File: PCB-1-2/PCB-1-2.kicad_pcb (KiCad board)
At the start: 2 copper layers, 89 x 51.5 mm, 97 parts, among them J1 Bus_PCI_Express_x8, J2 ST STDC14 (Debug Connector), J3 USB4105-GF-A, U1 LTC1298IS8_PBF, U10 INA827AIDGKR, U11 LTC1250CS8-PBF, U12 REF3425MDBVTEP, U13 HI-3585APQI, U14 MAX764ESA, U2 LTC1451IS8-PBF, U3 HI-3110PSIF, U4 FT231XS-R, U5 STM32F103RBT6, U6 STWD100YNXWY3F, U7 ADP7104ACPZ-R7 (v3.3), U8 OPA2187IDGKR, U9 ADP7104ACPZ-R7 (5v), Y1 8MHz Crystal, Y2 ABM8-24.000MHz-10-B1U-T

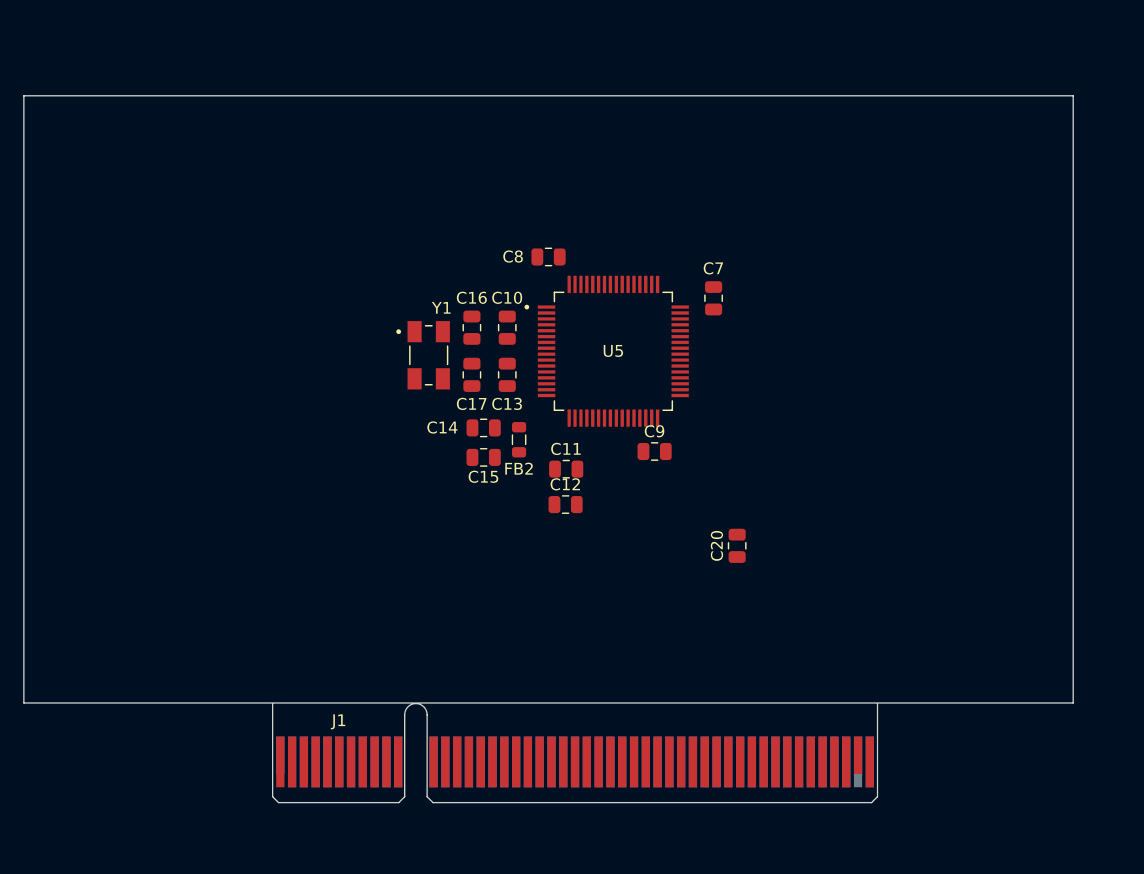
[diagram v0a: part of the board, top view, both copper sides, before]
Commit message: Fixing PCIe simple, not done yet
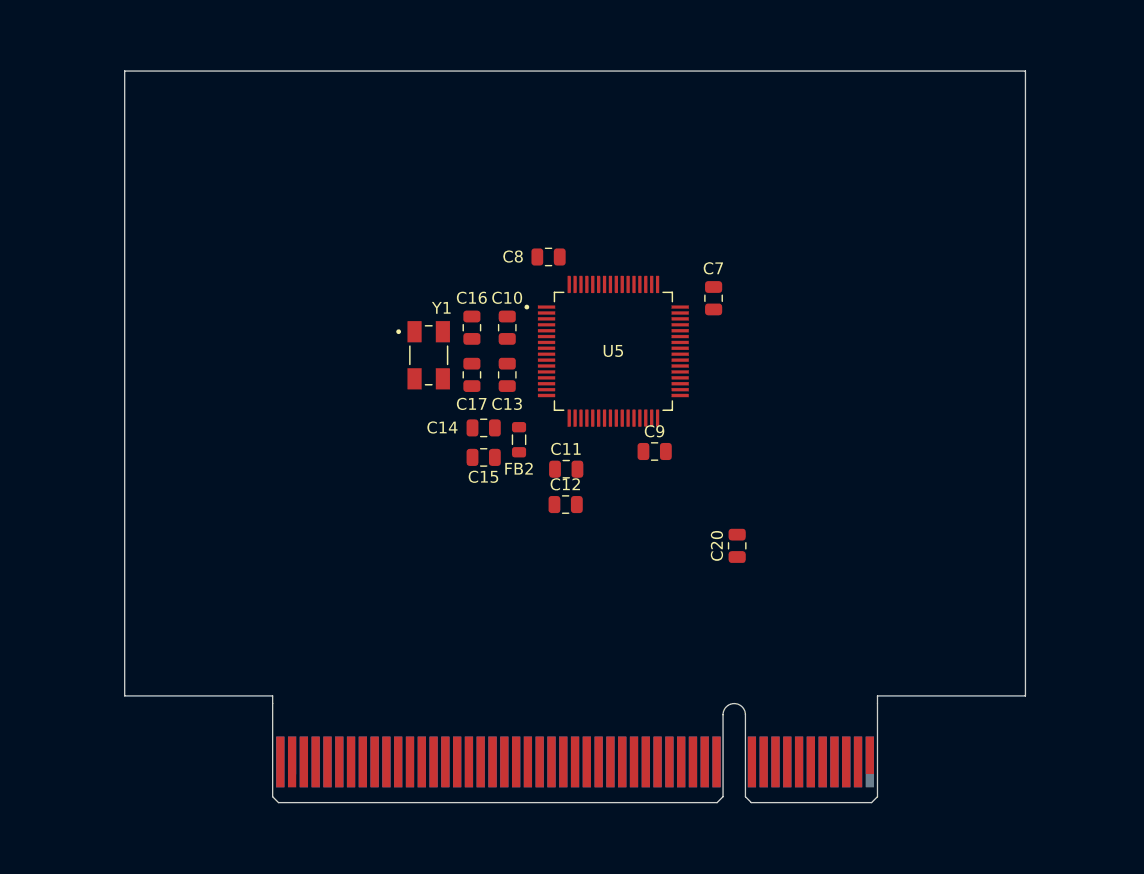
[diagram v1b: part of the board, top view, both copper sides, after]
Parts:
- C18, C19: value 4.7uF -> 22uF
- J1: moved to B.Cu
- moved J1 50.0 mm to (123.0, 131.0), turned to 180 degrees
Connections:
- C1 pad 2: GND -> Transducer-
- C10 pad 1: GND -> Transducer-
- C11 pad 1: GND -> Transducer-
- C12 pad 1: GND -> Transducer-
- C13 pad 2: GND -> Transducer-
- C14 pad 2: GND -> Transducer-
- C15 pad 2: GND -> Transducer-
- C16 pad 2: GND -> Transducer-
- C17 pad 2: GND -> Transducer-
- C18 pad 2: GND -> Transducer-
- C19 pad 2: GND -> Transducer-
- C2 pad 1: Net-(U2-VCC) -> +5V
- C2 pad 2: GND -> Transducer-
- C20 pad 2: GND -> Transducer-
- C21 pad 2: GND -> Transducer-
- C22 pad 2: GND -> Transducer-
- C23 pad 2: GND -> Transducer-
- C24 pad 1: GND -> Transducer-
- C26 pad 2: GND -> Transducer-
- C27 pad 2: GND -> Transducer-
- C28 pad 2: GND -> Transducer-
- C3 pad 2: GND -> Transducer-
- C30 pad 2: GND -> Transducer-
- C31 pad 2: GND -> Transducer-
- C32 pad 2: GND -> Transducer-
- C33 pad 2: GND -> Transducer-
- C34 pad 2: GND -> Transducer-
- C35 pad 2: GND -> Transducer-
- C36 pad 1: GND -> Transducer-
- C37 pad 1: GND -> Transducer-
- C38 pad 1: GND -> Transducer-
- C39 pad 2: GND -> Transducer-
- C4 pad 2: GND -> Transducer-
- C40 pad 2: GND -> Transducer-
- C41 pad 2: GND -> Transducer-
- C42 pad 1: GND -> Transducer-
- C43 pad 1: GND -> Transducer-
- C44 pad 1: GND -> Transducer-
- C45 pad 2: GND -> Transducer-
- C46 pad 2: GND -> Transducer-
- C5 pad 2: GND -> Transducer-
- C6 pad 1: GND -> Transducer-
- C7 pad 1: GND -> Transducer-
- C8 pad 1: GND -> Transducer-
- C9 pad 1: GND -> Transducer-
- D1 pad 1: GND -> Transducer-
- J2 pad 05: GND -> Transducer-
- J2 pad 07: GND -> Transducer-
- J2 pad 11: GND -> Transducer-
- J3 pad A1_B12: GND -> Transducer-
- J3 pad B1_A12: GND -> Transducer-
- J3 pad SH1: GND -> Transducer-
- J3 pad SH2: GND -> Transducer-
- J3 pad SH3: GND -> Transducer-
- J3 pad SH4: GND -> Transducer-
- R1 pad 2: GND -> Transducer-
- R18 pad 2: GND -> Transducer-
- R24 pad 2: GND -> Transducer-
- R25 pad 2: GND -> Transducer-
- R26 pad 2: GND -> Transducer-
- R7 pad 1: GND -> Transducer-
- R9 pad 1: GND -> Transducer-
- U1 pad 1: SPI1_CS -> SPI2_CS
- U1 pad 4: GND -> Transducer-
- U10 pad 5: GND -> Transducer-
- U10 pad 6: GND -> Transducer-
- U11 pad 4: GND -> Transducer-
- U12 pad 1: GND -> Transducer-
- U12 pad 2: GND -> Transducer-
- U13 pad 9: SPI1_CS -> SPI2_CS
- U14 pad 1: unconnected-(U14-OUT-Pad1) -> -5V
- U14 pad 2: unconnected-(U14-FB-Pad2) -> Net-(U14-FB)
- U14 pad 3: unconnected-(U14-SHDN-Pad3) -> Transducer-
- U14 pad 4: unconnected-(U14-REF-Pad4) -> Net-(U14-FB)
- U14 pad 5: unconnected-(U14-GND-Pad5) -> Transducer-
- U14 pad 6: unconnected-(U14-V+-Pad6) -> +5V
- U14 pad 7: unconnected-(U14-V+-Pad7) -> +5V
- U14 pad 8: unconnected-(U14-LX-Pad8) -> Net-(D2-K)
- U2 pad 3: SPI1_CS -> SPI2_CS
- U2 pad 5: GND -> Transducer-
- U2 pad 8: Net-(U2-VCC) -> +5V
- U3 pad 8: GND -> Transducer-
- U4 pad 16: GND -> Transducer-
- U4 pad 6: GND -> Transducer-
- U5 pad 12: GND -> Transducer-
- U5 pad 18: GND -> Transducer-
- U5 pad 31: GND -> Transducer-
- U5 pad 33: SPI1_CS -> SPI2_CS
- U5 pad 34: SPI2_CLK -> SPI2_SCK
- U5 pad 47: GND -> Transducer-
- U5 pad 60: GND -> Transducer-
- U5 pad 63: GND -> Transducer-
- U6 pad 2: GND -> Transducer-
- U7 pad 3: GND -> Transducer-
- U7 pad 6: GND -> Transducer-
- U7 pad 9: GND -> Transducer-
- U8 pad 4: GND -> Transducer-
- U9 pad 3: GND -> Transducer-
- U9 pad 6: GND -> Transducer-
- U9 pad 9: GND -> Transducer-
- Y1 pad 2: GND -> Transducer-
- Y1 pad 4: GND -> Transducer-
- Y2 pad 2: GND -> Transducer-
- Y2 pad 4: GND -> Transducer-
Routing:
- net Transducer-: track 0.00 -> 13.0 mm
- net GND: track 13.0 -> 0.00 mm
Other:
- board size 89 x 51.5 mm -> 76.4 x 53.6 mm
- copper layers 2 -> 4

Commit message: Merged both -1/-2 and backplane
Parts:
- removed the R1 at (111.3, 54.8)
- added C47: .1uF, Capacitor_SMD:C_0603_1608Metric, F.Cu at (95.1, 74.6)
- added C48: 22uF, Capacitor_SMD:C_0805_2012Metric, F.Cu at (93.7, 68.1)
- added C49: 22uF, Capacitor_SMD:C_0805_2012Metric, B.Cu at (93.6, 68.1)
- added C50: .1uF, Capacitor_SMD:C_0603_1608Metric, F.Cu at (106.1, 75.4)
- added C51: 10uF, Capacitor_SMD:C_1206_3216Metric, B.Cu at (110.6, 70.6)
- added C52: 22uF, Capacitor_SMD:C_0805_2012Metric, F.Cu at (93.6, 71.6)
- added C53: 2.2uF, Capacitor_SMD:C_0805_2012Metric, B.Cu at (93.6, 71.6)
- added C54: 22uF, Capacitor_SMD:C_0805_2012Metric, F.Cu at (106.2, 72.1)
- added C55: 200pF, Capacitor_SMD:C_0603_1608Metric, B.Cu at (131.0, 106.5)
- added C56: 20pF, Capacitor_SMD:C_0805_2012Metric, B.Cu at (124.6, 103.8)
- added C57: 20pF, Capacitor_SMD:C_0805_2012Metric, F.Cu at (133.5, 103.7)
- added C58: 330nF, Capacitor_SMD:C_0805_2012Metric, B.Cu at (121.5, 123.5)
- added C59: 22uF, Capacitor_SMD:C_0805_2012Metric, B.Cu at (106.1, 72.1)
- added C60: 22uF, Capacitor_SMD:C_0805_2012Metric, F.Cu at (106.1, 68.6)
- added C61: 22uF, Capacitor_SMD:C_0805_2012Metric, B.Cu at (106.1, 68.6)
- added C62: 22uF, Capacitor_SMD:C_0805_2012Metric, F.Cu at (110.1, 70.6)
- added D2: 1N5817, SDII LIB:1N5817, F.Cu at (106.5, 64.1)
- added D3: LED, LED_SMD:LED_0805_2012Metric, F.Cu at (76.8, 72.0)
- added D4: LED, LED_SMD:LED_0805_2012Metric, F.Cu at (82.6, 73.8)
- added D5: GPIO_LED, LED_SMD:LED_0805_2012Metric, F.Cu at (107.5, 106.5)
- added FB1: 120R, Inductor_SMD:L_0805_2012Metric, B.Cu at (76.6, 68.1)
- added H1: MountingHole, MountingHole:MountingHole_2.2mm_M2, F.Cu at (134.7, 124.0)
- added H2: MountingHole, MountingHole:MountingHole_2.2mm_M2, F.Cu at (61.2, 123.9)
- added H3: MountingHole, MountingHole:MountingHole_2.2mm_M2, F.Cu at (134.7, 61.5)
- added H4: MountingHole, MountingHole:MountingHole_2.2mm_M2, F.Cu at (61.2, 61.4)
- added J4: Conn_01x02_Pin, SDII LIB:pin header, F.Cu at (61.5, 100.5)
- added L2: 47uH, LED_SMD:LED_0805_2012Metric, F.Cu at (102.2, 67.5)
- added R28: 1.2k, Resistor_SMD:R_0805_2012Metric, F.Cu at (107.5, 103.0)
- added R30: 30, Resistor_SMD:R_0603_1608Metric, F.Cu at (65.0, 97.0)
- added R31: 30, Resistor_SMD:R_0603_1608Metric, F.Cu at (65.0, 107.0)
- added R32: 30, Resistor_SMD:R_0603_1608Metric, B.Cu at (65.0, 97.0)
- added R33: 30, Resistor_SMD:R_0603_1608Metric, B.Cu at (65.0, 107.0)
- C10, C11, C12, C13, C14, C15, C20, C38, C39, C4, C40, C41, C42, C43, C44, C5, FB2, R1, R10, R12, R15, R17, R19, R21, R22, R24, R25, R26, R27, R29, R4, R5, R6, R8, U6: moved to B.Cu
- C22: value 332nF -> 2nF; footprint Capacitor_SMD:C_0805_2012Metric -> Capacitor_SMD:C_0603_1608Metric
- C23: footprint Capacitor_SMD:C_0805_2012Metric -> Capacitor_SMD:C_0402_1005Metric
- C29: value 400pF -> 200pF; footprint Capacitor_SMD:C_0805_2012Metric -> Capacitor_SMD:C_0603_1608Metric
- C30, C31: value 40pF -> 20pF
- R34: renamed from R28; value 2k -> 1.2k
- moved C38 225.9 mm to (88.2, 94.9), turned to -135 degrees
- moved U6 223.7 mm to (90.5, 97.0), turned to -135 degrees
- moved R27 211.8 mm to (96.5, 90.0), turned to -135 degrees
- moved R34 207.8 mm to (63.0, 73.4), turned to -90 degrees
- moved D1 205.3 mm to (63.0, 76.9), turned to 90 degrees
- moved U14 203.3 mm to (97.5, 69.7)
- moved R10 178.6 mm to (106.1, 121.0), turned to 180 degrees
- moved U7 177.0 mm to (106.1, 120.9), turned to -90 degrees
- moved C19 171.7 mm to (105.9, 117.7), turned to 180 degrees
- moved R8 168.7 mm to (106.6, 116.7), turned to -90 degrees
- moved R9 167.2 mm to (105.9, 115.7), turned to 0 degrees
- moved R5 163.5 mm to (110.4, 120.9), turned to 180 degrees
- moved U9 162.4 mm to (110.3, 120.9), turned to -90 degrees
- moved C18 157.3 mm to (110.1, 117.6), turned to 180 degrees
- moved R6 153.9 mm to (111.0, 116.6), turned to -90 degrees
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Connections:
- C1 pad 2: Transducer- -> GND
- C10 pad 1: Transducer- -> GND
- C11 pad 1: Transducer- -> GND
- C12 pad 1: Transducer- -> GND
- C13 pad 2: Transducer- -> GND
- C14 pad 2: Transducer- -> GND
- C15 pad 2: Transducer- -> GND
- C16 pad 2: Transducer- -> GND
- C17 pad 2: Transducer- -> GND
- C18 pad 2: Transducer- -> GND
- C19 pad 2: Transducer- -> GND
- C2 pad 2: Transducer- -> GND
- C20 pad 2: Transducer- -> GND
- C21 pad 2: Transducer- -> GND
- C22 pad 2: Transducer- -> GND
- C23 pad 2: Transducer- -> GND
- C24 pad 1: Transducer- -> GND
- C26 pad 2: Transducer- -> GND
- C27 pad 2: Transducer- -> GND
- C28 pad 2: Transducer- -> GND
- C3 pad 2: Transducer- -> GND
- C30 pad 2: Transducer- -> GND
- C31 pad 2: Transducer- -> GND
- C32 pad 2: Transducer- -> GND
- C33 pad 2: Transducer- -> GND
- C34 pad 2: Transducer- -> GND
- C35 pad 2: Transducer- -> GND
- C36 pad 1: Transducer- -> GND
- C37 pad 1: Transducer- -> GND
- C38 pad 1: Transducer- -> GND
- C39 pad 2: Transducer- -> GND
- C4 pad 2: Transducer- -> GND
- C40 pad 2: Transducer- -> GND
- C41 pad 2: Transducer- -> GND
- C42 pad 1: Transducer- -> GND
- C43 pad 1: Transducer- -> GND
- C44 pad 1: Transducer- -> GND
- C45 pad 2: Transducer- -> GND
- C46 pad 2: Transducer- -> GND
- C5 pad 2: Transducer- -> GND
- C6 pad 1: Transducer- -> GND
- C7 pad 1: Transducer- -> GND
- C8 pad 1: Transducer- -> GND
- C9 pad 1: Transducer- -> GND
- D1 pad 1: Transducer- -> GND
- J1 pad A10: Net-(J1-+3.3V-PadA10) -> 429_IN-
- J1 pad A11: unconnected-(J1-~{PERST}-PadA11) -> 429_IN+
- J1 pad A12: Net-(J1-GND-PadA12) -> 429_OUT+
- J1 pad A13: unconnected-(J1-REFCLK+-PadA13) -> 429_OUT-
- J1 pad A15: Net-(J1-GND-PadA12) -> unconnected-(J1-Serial-PadA15)
- J1 pad A16: unconnected-(J1-PERp0-PadA16) -> GND
- J1 pad A17: unconnected-(J1-PERn0-PadA17) -> V+_FROM_PCIE
- J1 pad A18: Net-(J1-GND-PadA12) -> GND
- J1 pad A19: unconnected-(J1-RSVD-PadA19) -> DISCRETE_INPUT_1
- J1 pad A2: Net-(J1-+12V-PadA2) -> Transducer+
- J1 pad A20: Net-(J1-GND-PadA12) -> DISCRETE_INPUT_2
- J1 pad A21: unconnected-(J1-PERp1-PadA21) -> DISCRETE_INPUT_3
- J1 pad A22: unconnected-(J1-PERn1-PadA22) -> DISCRETE_INPUT_4
- J1 pad A23: Net-(J1-GND-PadA12) -> DISCRETE_INPUT_5
- J1 pad A24: Net-(J1-GND-PadA12) -> DISCRETE_INPUT_6
- J1 pad A25: unconnected-(J1-PERp2-PadA25) -> GND
- J1 pad A26: unconnected-(J1-PERn2-PadA26) -> GND
- J1 pad A27: Net-(J1-GND-PadA12) -> DISCRETE_OUTPUT_1
- J1 pad A28: Net-(J1-GND-PadA12) -> DISCRETE_OUTPUT_2
- J1 pad A29: unconnected-(J1-PERp3-PadA29) -> DISCRETE_OUTPUT_3
- J1 pad A3: Net-(J1-+12V-PadA2) -> RTD-
- J1 pad A30: unconnected-(J1-PERn3-PadA30) -> DISCRETE_OUTPUT_4
- J1 pad A31: Net-(J1-GND-PadA12) -> DISCRETE_OUTPUT_5
- J1 pad A32: unconnected-(J1-RSVD-PadA32) -> DISCRETE_OUTPUT_6
- J1 pad A33: unconnected-(J1-RSVD-PadA33) -> GND
- J1 pad A34: Net-(J1-GND-PadA12) -> HW_ID_1
- J1 pad A35: unconnected-(J1-PERp4-PadA35) -> HW_ID_2
- J1 pad A36: unconnected-(J1-PERn4-PadA36) -> HW_ID_3
- J1 pad A37: Net-(J1-GND-PadA12) -> unconnected-(J1-GND-PadA37)
- J1 pad A38: Net-(J1-GND-PadA12) -> unconnected-(J1-GND-PadA38)
- J1 pad A4: Net-(J1-GND-PadA12) -> RTD+
- J1 pad A41: Net-(J1-GND-PadA12) -> unconnected-(J1-GND-PadA41)
- J1 pad A42: Net-(J1-GND-PadA12) -> unconnected-(J1-GND-PadA42)
- J1 pad A45: Net-(J1-GND-PadA12) -> unconnected-(J1-GND-PadA45)
- J1 pad A46: Net-(J1-GND-PadA12) -> unconnected-(J1-GND-PadA46)
- J1 pad A49: Net-(J1-GND-PadA12) -> unconnected-(J1-GND-PadA49)
- J1 pad A5: unconnected-(J1-JTAG2-PadA5) -> DAC_OUT
- J1 pad A6: unconnected-(J1-JTAG3-PadA6) -> GND
- J1 pad A7: unconnected-(J1-JTAG4-PadA7) -> 825_CANL
- J1 pad A8: unconnected-(J1-JTAG5-PadA8) -> 825_CANH
- J1 pad A9: Net-(J1-+3.3V-PadA10) -> GND
- J1 pad B1: Net-(J1-+12V-PadA2) -> NC
- J1 pad B10: unconnected-(J1-3.3Vaux-PadB10) -> NC
- J1 pad B13: Net-(J1-GND-PadA12) -> unconnected-(J1-GND-PadB13)
- J1 pad B16: Net-(J1-GND-PadA12) -> unconnected-(J1-GND-PadB16)
- J1 pad B18: Net-(J1-GND-PadA12) -> unconnected-(J1-GND-PadB18)
- J1 pad B2: Net-(J1-+12V-PadA2) -> unconnected-(J1-NC-PadB2)
- J1 pad B21: Net-(J1-GND-PadA12) -> unconnected-(J1-GND-PadB21)
- J1 pad B22: Net-(J1-GND-PadA12) -> unconnected-(J1-GND-PadB22)
- J1 pad B25: Net-(J1-GND-PadA12) -> unconnected-(J1-GND-PadB25)
- J1 pad B26: Net-(J1-GND-PadA12) -> unconnected-(J1-GND-PadB26)
- J1 pad B29: Net-(J1-GND-PadA12) -> unconnected-(J1-GND-PadB29)
- J1 pad B3: Net-(J1-+12V-PadA2) -> unconnected-(J1-NC-PadB3)
- J1 pad B32: Net-(J1-GND-PadA12) -> unconnected-(J1-GND-PadB32)
- J1 pad B35: Net-(J1-GND-PadA12) -> unconnected-(J1-GND-PadB35)
- J1 pad B36: Net-(J1-GND-PadA12) -> unconnected-(J1-GND-PadB36)
- J1 pad B39: Net-(J1-GND-PadA12) -> unconnected-(J1-GND-PadB39)
- J1 pad B4: Net-(J1-GND-PadA12) -> GND
- J1 pad B40: Net-(J1-GND-PadA12) -> unconnected-(J1-GND-PadB40)
- J1 pad B43: Net-(J1-GND-PadA12) -> unconnected-(J1-GND-PadB43)
- J1 pad B44: Net-(J1-GND-PadA12) -> unconnected-(J1-GND-PadB44)
- J1 pad B47: Net-(J1-GND-PadA12) -> unconnected-(J1-GND-PadB47)
- J1 pad B49: Net-(J1-GND-PadA12) -> unconnected-(J1-GND-PadB49)
- J1 pad B7: Net-(J1-GND-PadA12) -> unconnected-(J1-GND-PadB7)
- J1 pad B8: Net-(J1-+3.3V-PadA10) -> NC
- J2 pad 05: Transducer- -> GND
- J2 pad 07: Transducer- -> GND
- J2 pad 11: Transducer- -> GND
- J3 pad A1_B12: Transducer- -> GND
- J3 pad B1_A12: Transducer- -> GND
- J3 pad SH1: Transducer- -> GND
- J3 pad SH2: Transducer- -> GND
- J3 pad SH3: Transducer- -> GND
- J3 pad SH4: Transducer- -> GND
- R1 pad 2: Transducer- -> GND
- R18 pad 2: Transducer- -> GND
- R24 pad 2: Transducer- -> GND
- R25 pad 2: Transducer- -> GND
- R26 pad 2: Transducer- -> GND
- R5 pad 1: +5V -> Net-(U9-PG)
- R5 pad 2: Net-(U9-PG) -> +5V
- R7 pad 1: Transducer- -> GND
- R9 pad 1: Transducer- -> GND
- U1 pad 4: Transducer- -> GND
- U10 pad 5: Transducer- -> GND
- U10 pad 6: Transducer- -> GND
- U11 pad 4: Transducer- -> GND
- U12 pad 1: Transducer- -> GND
- U12 pad 2: Transducer- -> GND
- U14 pad 3: Transducer- -> GND
- U14 pad 5: Transducer- -> GND
- U2 pad 5: Transducer- -> GND
- U3 pad 8: Transducer- -> GND
- U4 pad 16: Transducer- -> GND
- U4 pad 6: Transducer- -> GND
- U5 pad 10: DISCRETE_OUTPUT_3 -> DISCRETE_OUTPUT_4
- U5 pad 11: DISCRETE_OUTPUT_4 -> DISCRETE_OUTPUT_3
- U5 pad 12: Transducer- -> GND
- U5 pad 14: WD_WDI -> DISCRETE_OUTPUT_2
- U5 pad 15: WD_EN -> DISCRETE_OUTPUT_1
- U5 pad 18: Transducer- -> GND
- U5 pad 24: DISCRETE_OUTPUT_5 -> unconnected-(U5-PC4-Pad24)
- U5 pad 25: DISCRETE_OUTPUT_6 -> DISCRETE_INPUT_6
- U5 pad 26: ARINC_429_CLK -> DISCRETE_INPUT_5
- U5 pad 27: HW_ID_1 -> DISCRETE_INPUT_4
- U5 pad 28: HW_ID_2 -> DISCRETE_INPUT_3
- U5 pad 29: 429_RFLAG -> DISCRETE_INPUT_2
- U5 pad 30: 429_TFLAG -> DISCRETE_INPUT_1
- U5 pad 31: Transducer- -> GND
- U5 pad 37: DISCRETE_INPUT_1 -> Net-(U5-PC6)
- U5 pad 38: DISCRETE_INPUT_2 -> unconnected-(U5-PC7-Pad38)
- U5 pad 39: DISCRETE_INPUT_3 -> unconnected-(U5-PC8-Pad39)
- U5 pad 40: DISCRETE_INPUT_4 -> 429_RFLAG
- U5 pad 41: unconnected-(U5-PA8-Pad41) -> 429_TFLAG
- U5 pad 44: unconnected-(U5-PA11-Pad44) -> ARINC_429_CLK
- U5 pad 45: unconnected-(U5-PA12-Pad45) -> 429_MR
- U5 pad 47: Transducer- -> GND
- U5 pad 51: DISCRETE_INPUT_5 -> WD_EN
- U5 pad 52: DISCRETE_INPUT_6 -> WD_WDI
- U5 pad 53: 429_MR -> 825_STAT
- U5 pad 54: unconnected-(U5-PD2-Pad54) -> 825_TXEN
- U5 pad 55: HW_ID_3 -> 825_MR
- U5 pad 57: 825_MR -> 825_GP2
- U5 pad 59: 825_GP2 -> HW_ID_3
- U5 pad 60: Transducer- -> GND
- U5 pad 61: 825_TXEN -> HW_ID_2
- U5 pad 62: 825_STAT -> HW_ID_1
- U5 pad 63: Transducer- -> GND
- U5 pad 8: DISCRETE_OUTPUT_1 -> DISCRETE_OUTPUT_6
- U5 pad 9: DISCRETE_OUTPUT_2 -> DISCRETE_OUTPUT_5
- U6 pad 2: Transducer- -> GND
- U7 pad 3: Transducer- -> GND
- U7 pad 6: Transducer- -> GND
- U7 pad 9: Transducer- -> GND
- U8 pad 4: Transducer- -> GND
- U9 pad 3: Transducer- -> GND
- U9 pad 6: Transducer- -> GND
- U9 pad 9: Transducer- -> GND
- Y1 pad 2: Transducer- -> GND
- Y1 pad 4: Transducer- -> GND
- Y2 pad 2: Transducer- -> GND
- Y2 pad 4: Transducer- -> GND
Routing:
- net GND: track 0.00 -> 254.6 mm, vias 0 -> 131
- net 825_CANL: track 0.00 -> 88.3 mm, vias 0 -> 3
- net 825_CANH: track 0.00 -> 78.6 mm, vias 0 -> 3
- net DAC_OUT: track 0.00 -> 71.4 mm, vias 0 -> 4
- net USART2_TX: track 0.00 -> 59.6 mm, vias 0 -> 4
- net +3.3V: track 27.8 -> 87.1 mm, vias 0 -> 15
- net +5V: track 28.3 -> 86.1 mm, vias 0 -> 17
- net ADC_CH0: track 0.00 -> 54.6 mm, vias 0 -> 2
- net SPI2_CS: track 0.00 -> 54.4 mm, vias 0 -> 4
- net SPI2_MOSI: track 0.00 -> 53.5 mm, vias 0 -> 4
- net USART2_RX: track 0.00 -> 50.3 mm, vias 0 -> 4
- net HW_ID_3: track 0.00 -> 49.8 mm, vias 0 -> 6
- net SPI2_MISO: track 0.00 -> 49.7 mm, vias 0 -> 4
- net HW_ID_2: track 0.00 -> 49.2 mm, vias 0 -> 6
- net 429_OUT-: track 0.00 -> 49.1 mm
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- added copper zone on In2.Cu, net +3.3V
- added copper zone on In2.Cu, net +5V
- added copper zone on In2.Cu, net -5V
- added copper zone on In1.Cu, net GND
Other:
- board size 76.4 x 53.6 mm -> 76.4 x 66 mm

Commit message: Updated -1/-2 and added test jig
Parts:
- moved C15 6.04 mm to (95.5, 116.5), turned to -45 degrees
- moved C14 5.68 mm to (87.5, 116.5)
- moved Y2 2.42 mm to (77.7, 90.1)
- moved H2 1.61 mm to (62.4, 122.8)
- moved H4 1.60 mm to (62.4, 62.6)
- moved H3 1.57 mm to (133.6, 62.6)
- moved H1 1.56 mm to (133.6, 122.9)
- moved FB2 1.00 mm to (91.5, 117.5), turned to 45 degrees
- turned C12 to -135 degrees
- turned C9 to -135 degrees
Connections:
- C13 pad 1: +3.3V -> +3.3VA
- C14 pad 1: +3.3V -> +3.3VA
- FB2 pad 1: +3.3V -> +3.3VA
- U5 pad 13: +3.3V -> +3.3VA
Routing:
- net GND: track 254.6 -> 169.7 mm, vias 131 -> 137
- net +3.3V: track 87.1 -> 66.0 mm, vias 15 -> 14
- net +5V: track 86.1 -> 72.0 mm
- net +3.3VA: track 0.00 -> 10.1 mm, vias 0 -> 1
- net Net-(U3-OSCOUT): track 17.2 -> 20.1 mm, vias 1 -> 2
- net -5V: track 22.3 -> 21.0 mm
- net Net-(U3-OSCIN): track 10.7 -> 11.6 mm, vias 1 -> 2
- net DAC_OUT: track 71.4 -> 72.1 mm
- added copper zone on F.Cu, net GND
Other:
- board size 76.4 x 66 mm -> 76.4 x 66.5 mm

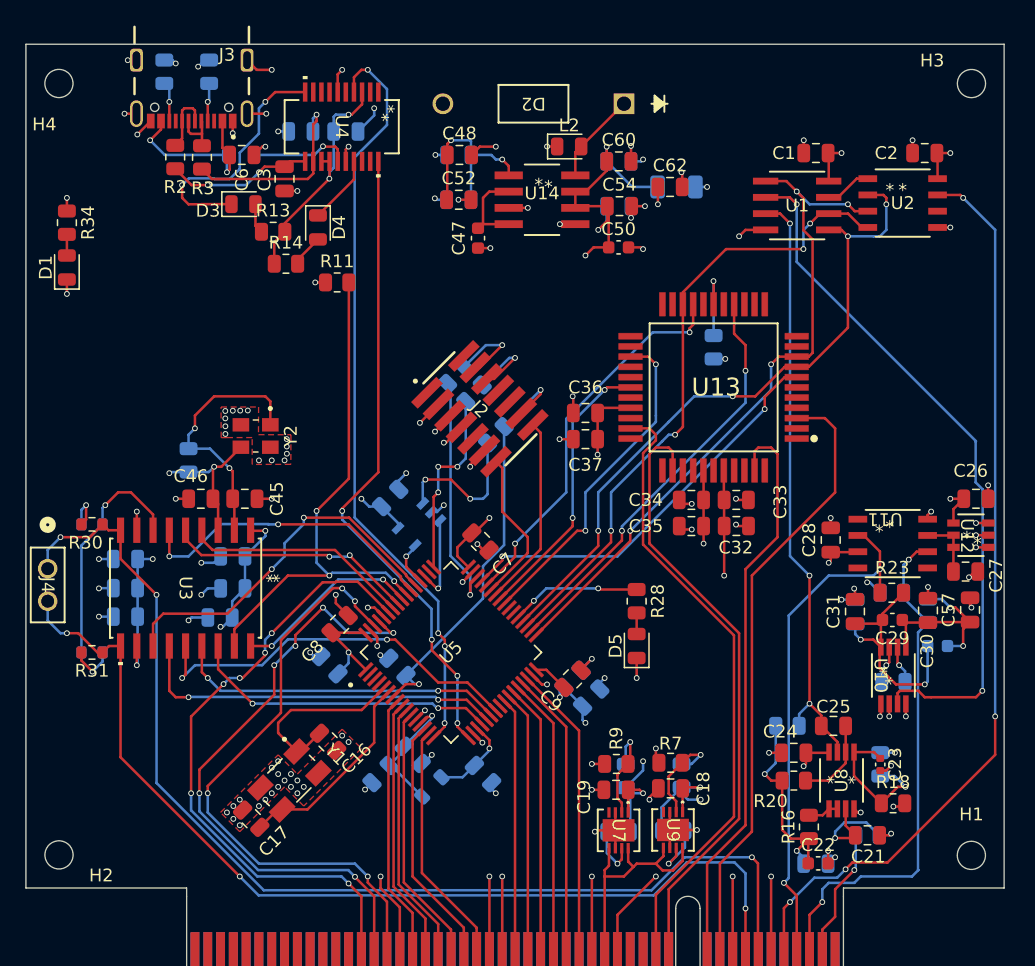
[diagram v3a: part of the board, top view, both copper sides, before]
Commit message: Changed mounting holes and finalized setup
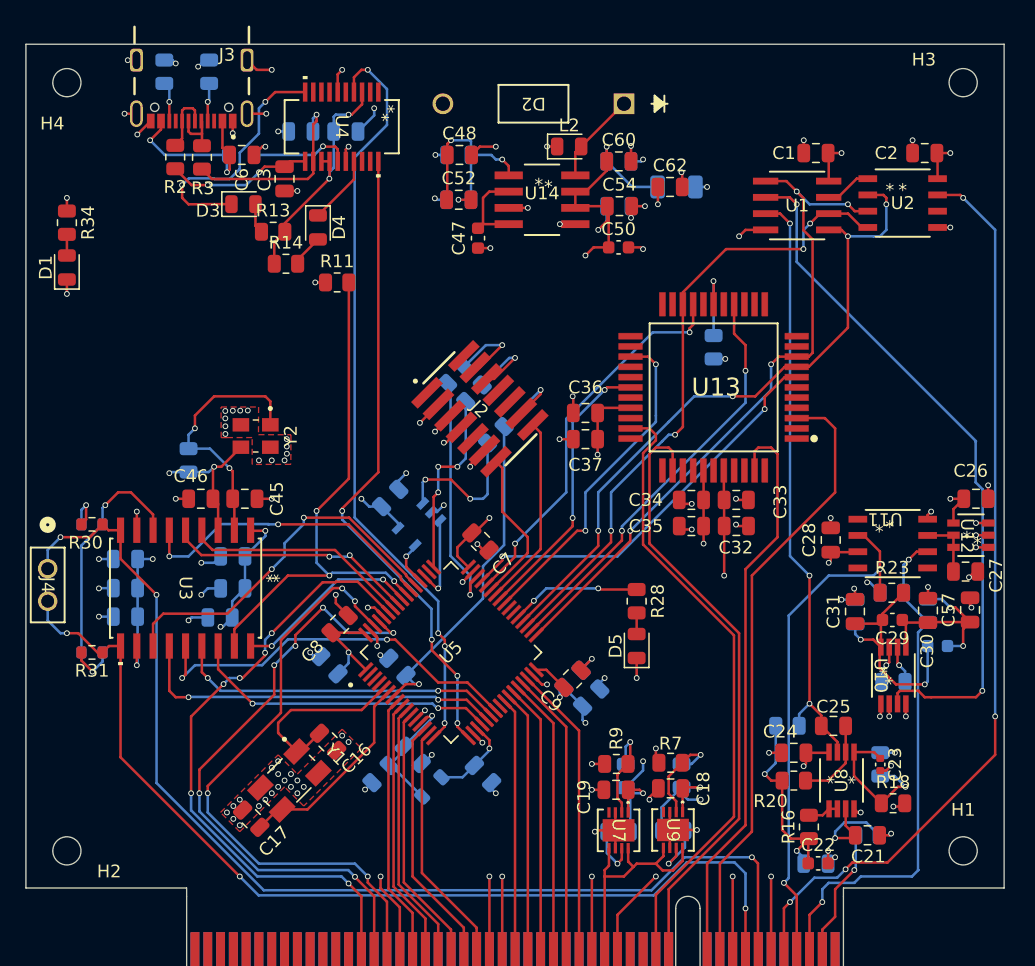
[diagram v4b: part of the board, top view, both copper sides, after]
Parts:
- moved H1 0.73 mm to (133.0, 122.5)
- moved H2 0.69 mm to (63.0, 122.5)
- moved H3 0.65 mm to (133.0, 62.5)
- moved H4 0.63 mm to (63.0, 62.5)
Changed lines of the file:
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@@
 	(footprint "MountingHole:MountingHole_2.2mm_M2"
 		(layer "F.Cu")
-		(at 133.648165 62.570366)
+		(at 133 62.5)
 		(descr "Mounting Hole 2.2mm, no annular, M2")
 		(tags "mounting hole 2.2mm no annular m2")
@@
 	(footprint "MountingHole:MountingHole_2.2mm_M2"
 		(layer "F.Cu")
-		(at 62.377623 62.564684)
+		(at 63 62.5)
 		(descr "Mounting Hole 2.2mm, no annular, M2")
 		(tags "mounting hole 2.2mm no annular m2")
@@
 	(footprint "MountingHole:MountingHole_2.2mm_M2"
 		(layer "F.Cu")
-		(at 62.383061 122.814297)
+		(at 63 122.5)
 		(descr "Mounting Hole 2.2mm, no annular, M2")
 		(tags "mounting hole 2.2mm no annular m2")
@@
 	(footprint "MountingHole:MountingHole_2.2mm_M2"
 		(layer "F.Cu")
-		(at 133.641026 122.850816)
+		(at 133 122.5)
 		(descr "Mounting Hole 2.2mm, no annular, M2")
 		(tags "mounting hole 2.2mm no annular m2")

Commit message: Addressed Tims comments before ordering
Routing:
- net GND: track 169.7 -> 177.4 mm, vias 137 -> 134
- net V+_FROM_PCIE: track 20.0 -> 12.7 mm, vias 0 -> 11
- net Net-(U3-OSCIN): track 11.6 -> 10.1 mm, vias 2 -> 1
- net 825_CANL: track 88.3 -> 87.5 mm, vias 3 -> 2
- net 825_CANH: vias 3 -> 2
- added copper zone on F.Cu, net V+_FROM_PCIE
- added copper zone on In2.Cu, net V+_FROM_PCIE
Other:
- board text added: "Contributors: Devin Marx Erick Rodriguez Harleigh Schneider"

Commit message: Added logo
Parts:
- added G***: LOGO, SDII LIB:Big_Logo, B.Cu at (71.0, 80.0)
